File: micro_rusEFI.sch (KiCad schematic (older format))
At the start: 57 parts, among them J12 Conn_01x01, J13 Conn_01x01, J3 Conn_01x01, J4 Conn_02x05_Counter_Clockwise, J5 Conn_01x01, U3 molex_48pin_MRE, U7 XC6206 3.3V

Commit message: Updated R2 in schematic. Looks like there is still a BOM creation issue. Per https://github.com/rusefi/hw_microRusEfi/issues/175
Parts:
- R2: LCSC C21189 -> (none); Manufacturer Uniroyal Elec -> DNP; Part # 0603WAF0000T5E -> DNP
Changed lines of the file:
@@
 F 2 "Resistor_SMD:R_0603_1608Metric" V 8730 6025 50  0001 C CNN
 F 3 "~" H 8800 6025 50  0001 C CNN
-F 4 "Uniroyal Elec" H 475 100 50  0001 C CNN "Manufacturer"
-F 5 "0603WAF0000T5E" H 475 100 50  0001 C CNN "Part #"
+F 4 "DNP" H 475 100 50  0001 C CNN "Manufacturer"
+F 5 "DNP" H 475 100 50  0001 C CNN "Part #"
 F 6 "" H 475 100 50  0001 C CNN "VEND"
 F 7 "" H 475 100 50  0001 C CNN "VEND#"
-F 8 "C21189" H 8800 6025 50  0001 C CNN "LCSC"
+F 8 "" H 8800 6025 50  0001 C CNN "LCSC"
 	1    8800 6025
 	0    1    1    0

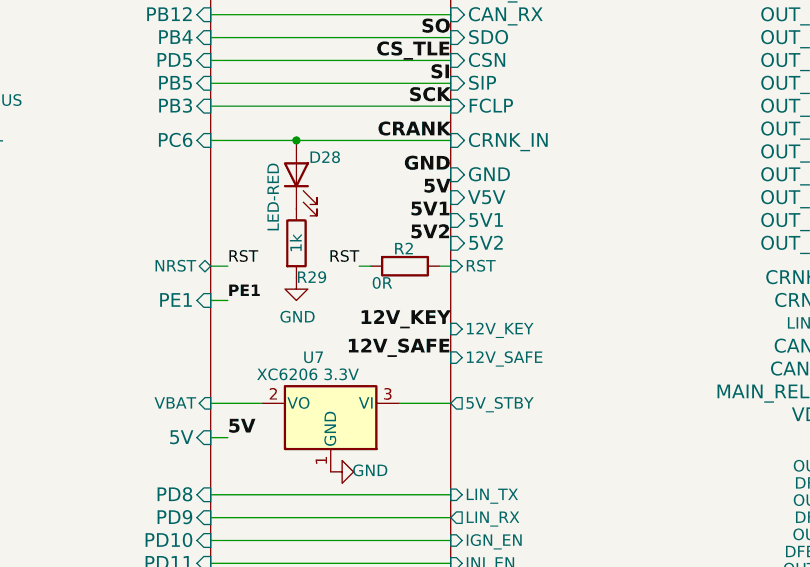
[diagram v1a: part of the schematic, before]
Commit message: Changed field name for long term DNP of R2 per https://github.com/rusefi/hw_microRusEfi/issues/175
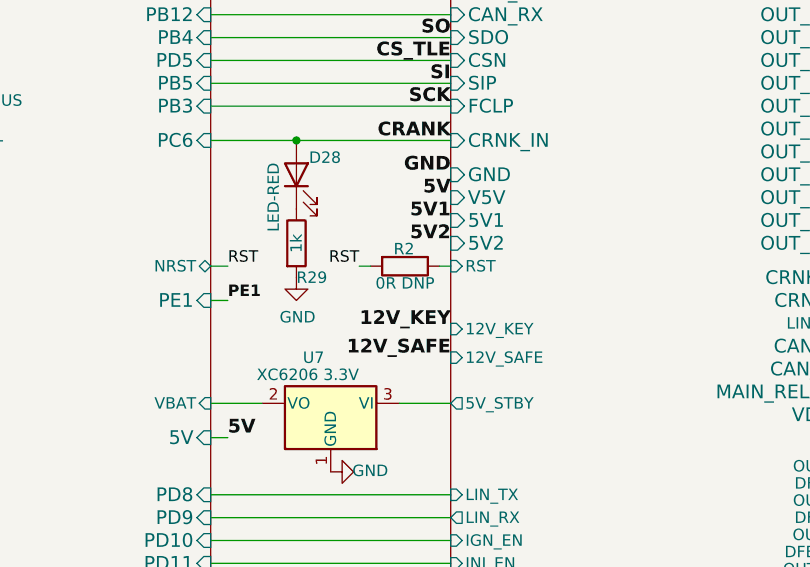
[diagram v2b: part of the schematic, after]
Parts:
- R2: value 0R -> 0R DNP
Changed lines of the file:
@@
 P 8800 6025
 F 0 "R2" V 8725 5975 50  0000 L CNN
-F 1 "0R" V 8875 5925 50  0000 C CNN
+F 1 "0R DNP" V 8875 6025 50  0000 C CNN
 F 2 "Resistor_SMD:R_0603_1608Metric" V 8730 6025 50  0001 C CNN
 F 3 "~" H 8800 6025 50  0001 C CNN

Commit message: squash
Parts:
- added D44: 1N4148WS, Diode_SMD:D_SOD-323, symbol micro_rusEFI-rescue:D_Schottky-Device
- added JP3: Voltage selector 5V 3V3, Jumper:SolderJumper-3_P1.3mm_Bridged12_RoundedPad1.0x1.5mm, symbol micro_rusEFI-rescue:SolderJumper_3_Open-Jumper
- added unit 18 of U3
- added unit 17 of U3
- added unit 19 of U3
- D15, D20, D3, D4, D5, D6, D7: symbol Device:D_Schottky -> micro_rusEFI-rescue:D_Schottky-Device
- D21, D22, D23, D27, D28, D31, D33, D35: symbol Device:LED -> micro_rusEFI-rescue:LED-Device
- D30, D32, D34, D43: symbol Device:D -> micro_rusEFI-rescue:D-Device
- D36, D37: symbol Diode:B340 -> micro_rusEFI-rescue:B340-Diode
- D41: symbol Device:D_TVS -> micro_rusEFI-rescue:D_TVS-Device
- J12, J13, J3, J5: symbol Connector_Generic:Conn_01x01 -> micro_rusEFI-rescue:Conn_01x01-Connector_Generic
- J4: symbol Connector_Generic:Conn_02x05_Odd_Even -> micro_rusEFI-rescue:Conn_02x05_Odd_Even-Connector_Generic
- LOGO1: symbol Graphic:Logo_Open_Hardware_Small -> micro_rusEFI-rescue:Logo_Open_Hardware_Small-Graphic
- NT2, NT3: symbol Device:Net-Tie_2 -> micro_rusEFI-rescue:Net-Tie_2-Device
- R10, R2, R21, R29, R30, R33, R36, R49, R51, R80, R81, R84, R85, R86: symbol Device:R -> micro_rusEFI-rescue:R-Device
- RN1: symbol Device:R_Pack04 -> micro_rusEFI-rescue:R_Pack04-Device
- TP0, TP1, TP12, TP2, TP3, TP4, TP5: symbol Connector:TestPoint -> micro_rusEFI-rescue:TestPoint-Connector
- U3: footprint rusefi_lib:Molex_48_MRE -> rusefi_lib:Molex_48_MRE_R055; symbol rusefi_Molex_MRE_Connector:molex_48pin_MRE -> micro_rusEFI-rescue:molex_48pin_MRE-rusefi_Molex_MRE_Connector
- U7: symbol Regulator_Linear:MCP1703A-3302_SOT23 -> micro_rusEFI-rescue:MCP1703A-3302_SOT23-Regulator_Linear
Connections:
- net 5V: now also JP3.3 (B)
- net CANH: now also U3.J22, U3.J49
- net CANL: now also U3.J23, U3.J50
- net GND: now also U3.J20
- net VDD: now also D44.2 (A)
- new net: D44.1 (K), JP3.1 (A)
- new net: JP3.2 (C), U3.J21
